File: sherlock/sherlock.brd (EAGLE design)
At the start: 91.4 x 58.4 mm, 28 parts, among them U3 XBEE-1B2, X1 2540-

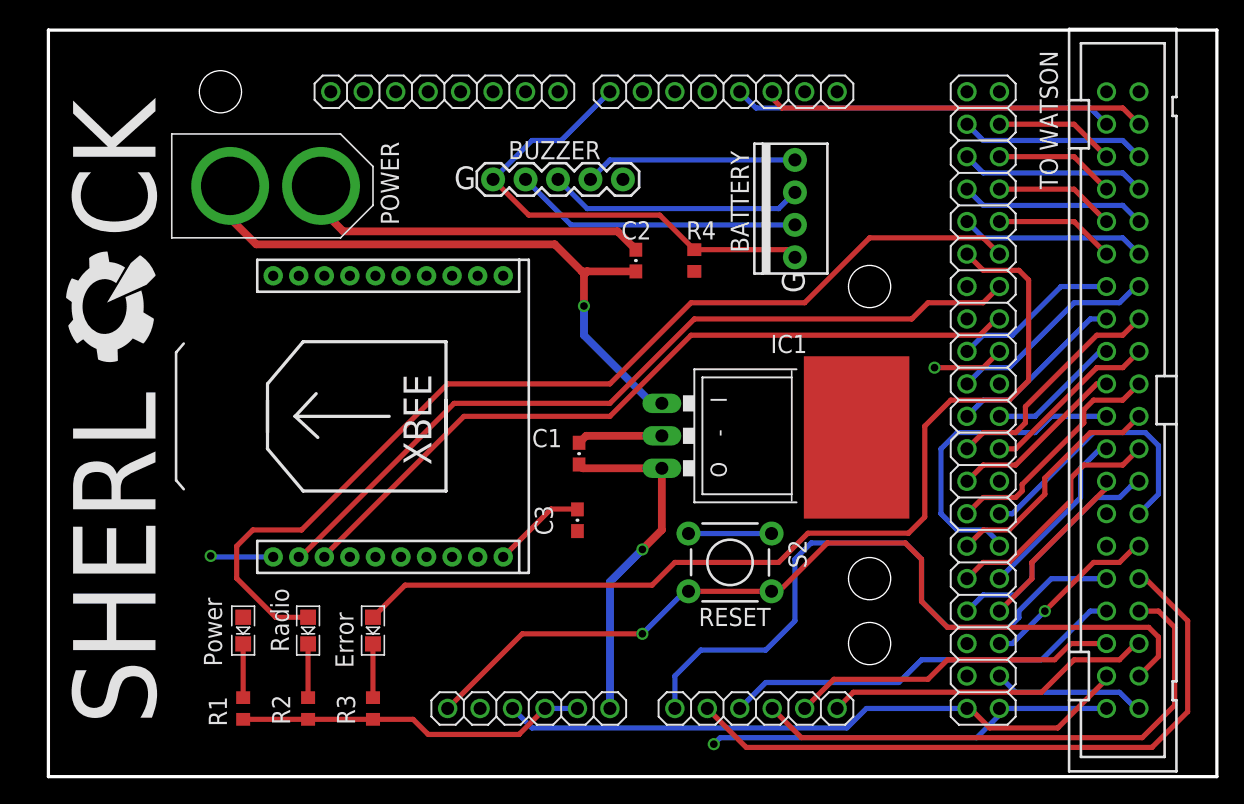
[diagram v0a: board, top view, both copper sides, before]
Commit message: Sherlock changes
buzzer grounded
holes fixed to fit Panda
silkscreen updated
random other stuff that was done before

Hopefully I do this right this time.
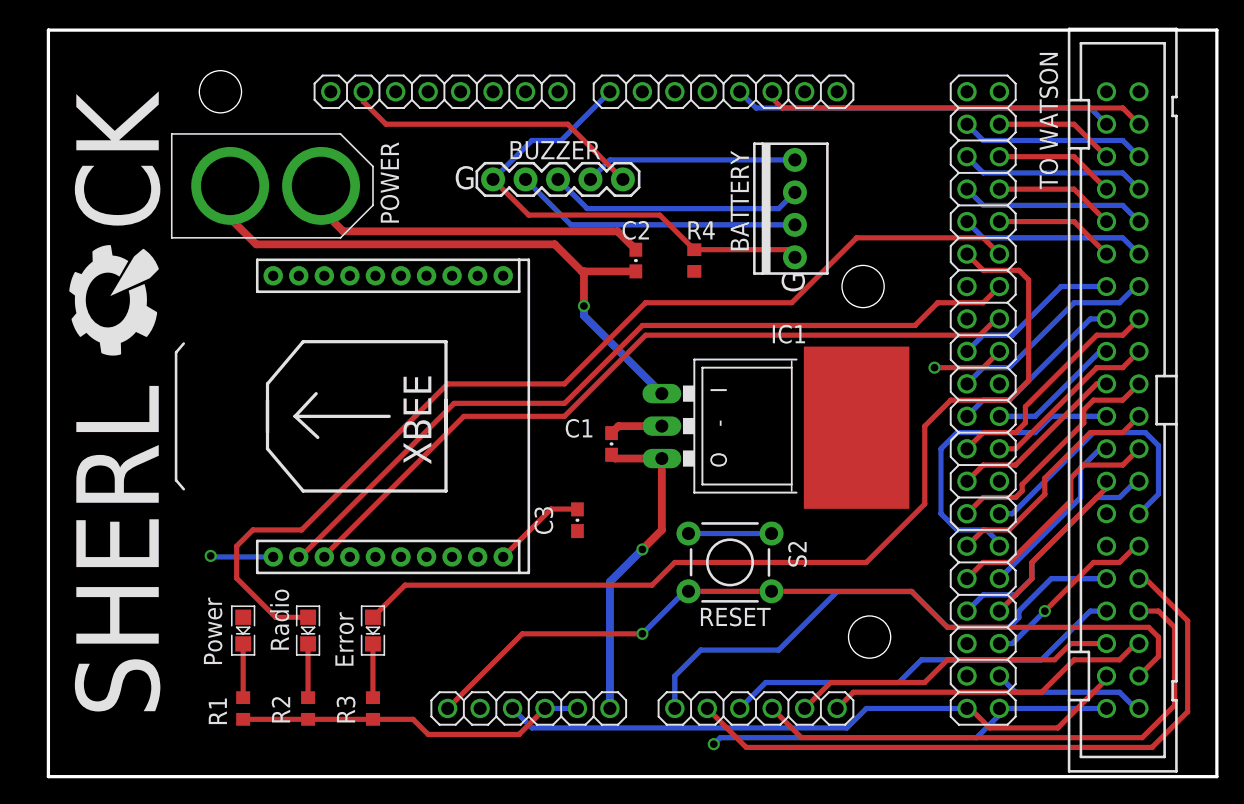
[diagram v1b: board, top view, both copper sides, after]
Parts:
- removed U$6: Test, pie:STAND-OFF
- moved U$5 66.7 mm to (13.5, 53.6)
- moved U$7 54.8 mm to (60.2, 28.4)
- moved U$3 52.6 mm to (63.8, 38.4)
- moved U$4 27.4 mm to (64.3, 10.9)
- moved C1 2.65 mm to (44.1, 26.0)
- moved IC1 0.76 mm to (56.9, 27.4)
- moved U$2 0.57 mm to (8.64, 4.57)
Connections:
- net GND: now also BUZZER.5
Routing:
- net GND: track 93.2 -> 114.2 mm
- net ADC0/IO28*: track 50.0 -> 42.1 mm
- net RESET#: track 69.7 -> 64.6 mm
- net VIN: track 27.1 -> 25.3 mm
- net 12V: track 49.4 -> 48.1 mm
- net IO60: track 76.7 -> 76.1 mm
- net ADC4/IO29: track 26.2 -> 25.7 mm
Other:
- board text added: "2013.10.13"
- board text added: "Copyright (c) 2013, Pioneers in Engineering All rights reserved. Design by: Sahar M, Michael C, Sumita G Yuting T, Aravind K This design is open source hardware. For more information, visit pioneers.berkeley.edu/opensource"
- board text added: "Sherlock V2.0 Rev A"
- board text removed: "2013.01.23"
- board text removed: "Copyright (c) 2013, Pioneers in Engineering All rights reserved. Design by: Sahar M., Michael C., and Sumita G. This design is open source hardware. For more information, visit pioneers.berkeley.edu/opensource"
- board text removed: "Sherlock V1.0 Rev F"

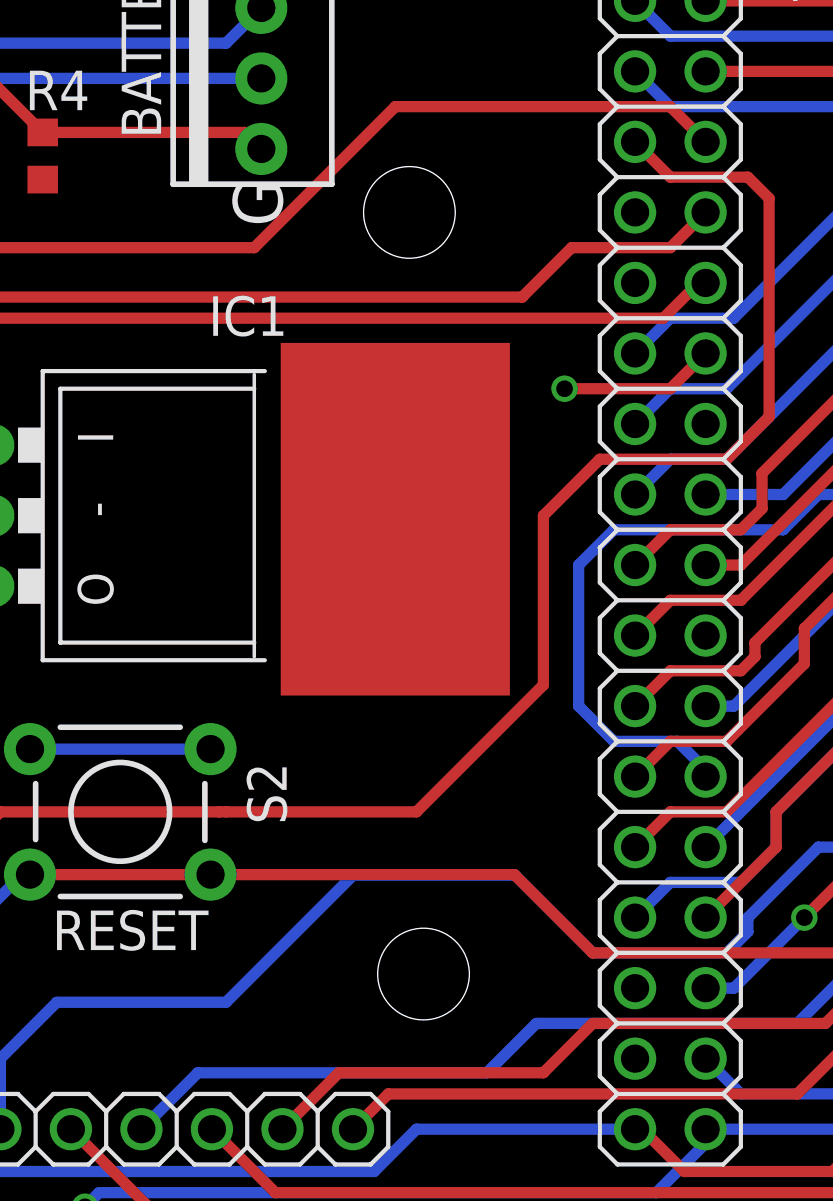
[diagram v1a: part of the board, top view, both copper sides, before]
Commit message: Sherlock
Symbols made consistent (carats for VCC, triangle for GND) ; names
added; holes fixed
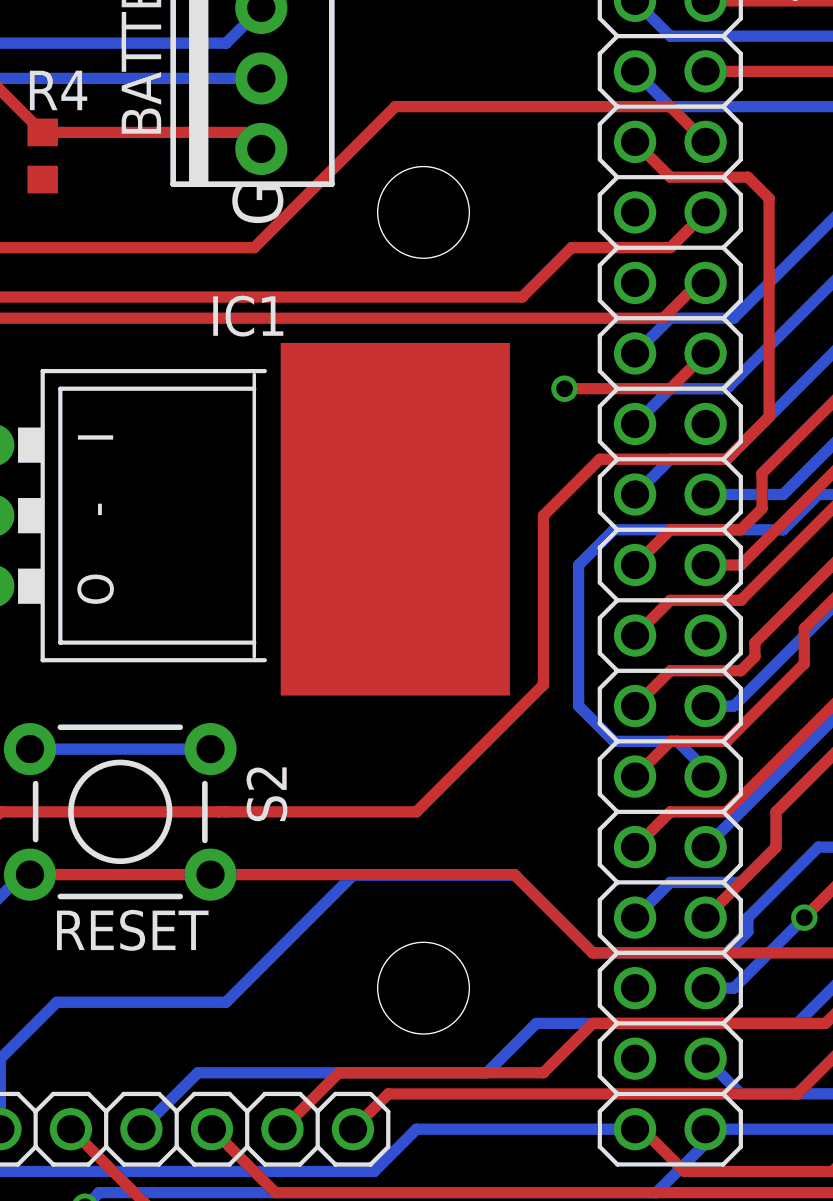
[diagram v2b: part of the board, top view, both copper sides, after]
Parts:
- moved U$3 0.51 mm to (64.3, 38.4)
- moved U$4 0.51 mm to (64.3, 10.4)
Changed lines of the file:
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@@
 <attribute name="VALUE" x="23.495" y="13.97" size="0.4064" layer="25" font="vector" rot="R270"/>
 </element>
-<element name="U$3" library="pie" package="STAND-OFF" value="Mounting + Test" x="63.754" y="38.354"/>
-<element name="U$4" library="pie" package="STAND-OFF" value="Mounting" x="64.262" y="10.922"/>
+<element name="U$3" library="pie" package="STAND-OFF" value="Mounting + Test" x="64.262" y="38.354"/>
+<element name="U$4" library="pie" package="STAND-OFF" value="Mounting" x="64.262" y="10.414"/>
 <element name="U$5" library="pie" package="STAND-OFF" value="Mounting" x="13.462" y="53.594"/>
 <element name="X1" library="pie" package="PAK100/2500-40" value="2540-" x="84.074" y="29.464" smashed="yes" rot="R90">
